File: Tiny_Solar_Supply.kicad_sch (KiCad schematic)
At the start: 16 parts, among them J1 Conn_01x02, J2 Conn_01x02, J3 Conn_01x02, J4 Conn_01x02, Q1 2N7002, U1 AP3015AKTR-G1

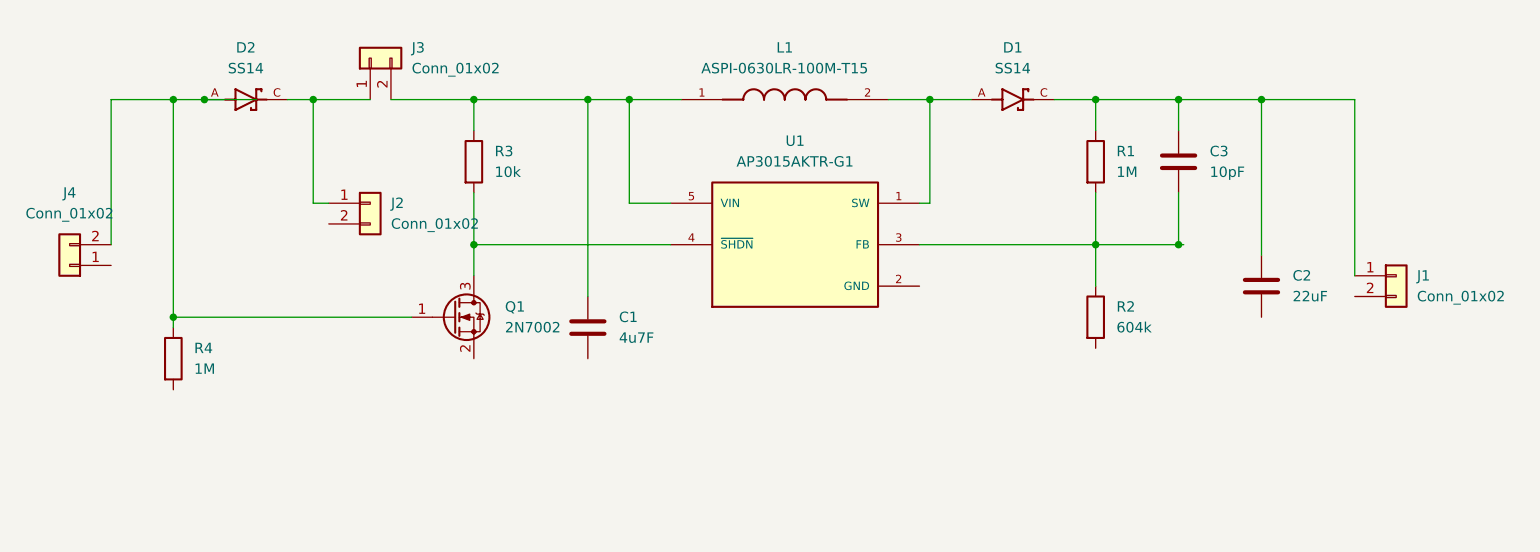
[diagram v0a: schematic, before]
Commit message: Schematic completed
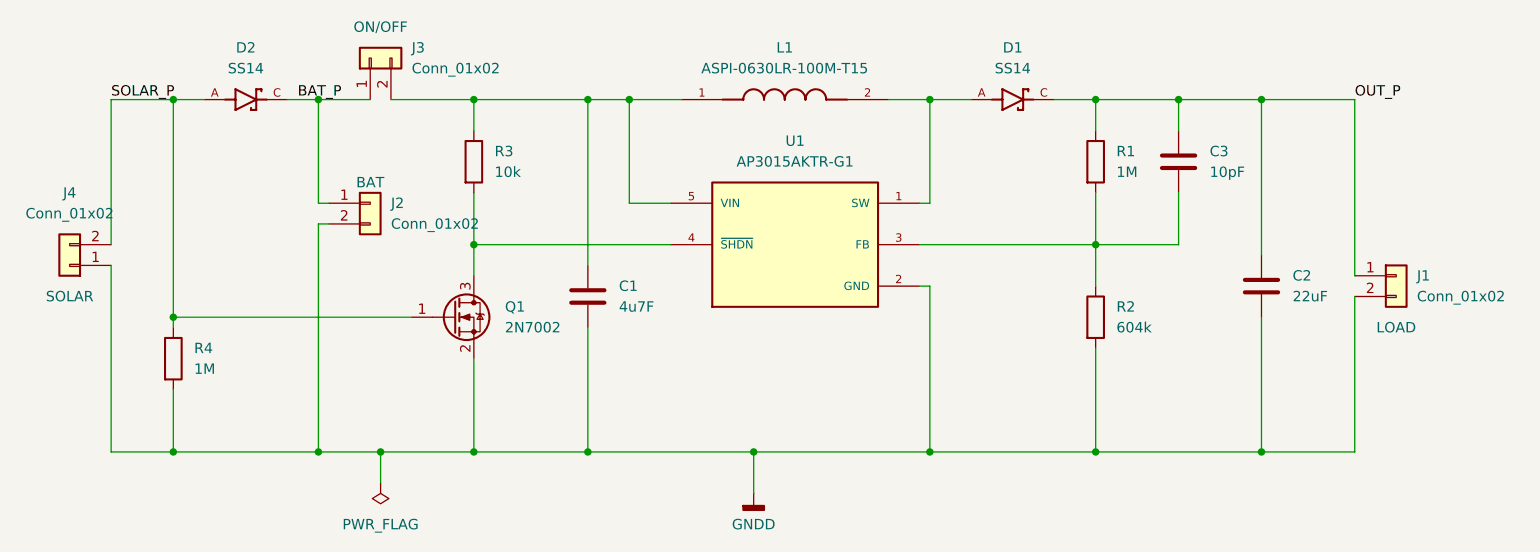
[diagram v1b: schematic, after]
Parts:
- J1: Short Description (none) -> LOAD
- J2: Short Description (none) -> BAT
- J3: Short Description (none) -> ON/OFF
- J4: Short Description (none) -> SOLAR
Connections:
- net SOLAR_P: now reaches D2.A, J4.2 (Pin_2), Q1.1 (G), R4.1
- net BAT_P: now reaches D2.C, J2.1 (Pin_1), J3.1 (Pin_1)
- net GNDD: now reaches C1.2
- net GNDD: now also C2.2, J1.2 (Pin_2), J2.2 (Pin_2), J4.1 (Pin_1), Q1.2 (S), R2.2, R4.2, U1.2 (GND)
- net OUT_P: now reaches C2.1, C3.1, D1.C, J1.1 (Pin_1), R1.1
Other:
- moved on the sheet: C1
